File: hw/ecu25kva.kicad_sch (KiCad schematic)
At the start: 0 parts

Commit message: Wire the root sheet: the project has a netlist for the first time
Ten sheets each passed their own netlist and the project had none. The
root sheet's ten sheet symbols carried NO hierarchical pins, so a net
name appearing on two sheets was two nets and nothing compared them --
the cross-sheet audit in the last commit was a name comparison, not a
connectivity check.

Each symbol now carries one pin per net its child exports, read OUT of
the child rather than declared in a second list that could drift: 162
pins across the ten, each with a stub and a label. Two labels with the
same name are one net, which is how 162 pins connect without routing
162 wires across a page nobody could read.

Exporting it found the other half of the same problem immediately.
kicad-cli reported annotation errors: every sheet generator allocated
R1, C1, U1 from its own counter, so ten sheets had ten parts called R1.
schlib.REF_BASE gives each sheet its own hundred -- KiCad's own
sheet-number x 100 convention, applied at generation time instead of by
a hand pass in Eeschema. 196 components, no duplicate reference.

hw/check_netlist.py is the gate, and the counterpart to sim/run_sim.py:
that one guards the component values, this one guards the connectivity.
Same rule -- an exemption is not a pass. Every single-pin net is listed
with its reason, and a net that STOPS being single-pin fails the check
until it is removed from the list. An open item that quietly closes is
as much a drift as one that quietly opens.

  196 components, every reference unique
  113 named nets carrying two or more pins
   18 named nets reaching one pin, each a recorded open item
      GND 134 pins, 3V3_MCU 27, VBAT_PROT 12 -- all spanning the project

The root sheet carries those eighteen on the page itself, grouped by
what they wait on, so a reader does not have to run a script to find
which ends are loose.

Full set plots to docs/pdf/ECU-Schematics.pdf, 11 pages.

Two rendering bugs fixed: sheet pin names and their stu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
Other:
- sheet can ports: added CAN1_H, CAN1_L, CAN1_RX, CAN1_TX, CAN2_H, CAN2_L, CAN2_RX, CAN2_TX; removed none
- sheet connector ports: added BOOST_P_IN, BOOST_T_IN, CAM_FREQ_46, CAM_GND_44, CAN1_H, CAN1_L, CAN2_H, CAN2_L, COOLANT_T_IN, CRANK_HI_52, CRANK_LO_74, EGR_HIGH_59, EGR_LOW_81, EGR_POS_IN, EXC_BOOST_11, EXC_CAM_45, EXC_EGR_15, EXC_OIL_39, EXC_RAIL_32, INJ_A_03, INJ_B_05, INJ_LS1_73, INJ_LS2_29, INJ_LS3_07, IN_AUDIO_ABORT_H, IN_IGNITION_H, IN_OVERRIDE_SS_H, MU_RETURN, OIL_P_IN, RAIL_P_IN, RLY_BUZZER_OUT, RLY_MAIN_OUT, SGND_34, SGND_36, SHIELD_30, SW_COOLANT_C, SW_DROOP_C, VBAT_IN, V_BAT_1R, V_BAT_2R; removed none
- sheet discrete_io ports: added IN_AUDIO_ABORT, IN_AUDIO_ABORT_H, IN_IGNITION, IN_IGNITION_H, IN_OVERRIDE_SS, IN_OVERRIDE_SS_H, RLY_BUZZER, RLY_BUZZER_OUT, RLY_MAIN, RLY_MAIN_OUT, SW_COOLANT, SW_COOLANT_C, SW_DROOP, SW_DROOP_C, TRIP_LOOP, TRIP_SENSE, VBAT_PROT; removed none
- sheet injector ports: added GATE_KILL, INJ_A_03, INJ_B_05, INJ_HS_A, INJ_HS_B, INJ_LS1_73, INJ_LS2_29, INJ_LS3_07, INJ_LS_1, INJ_LS_2, INJ_LS_3, VBAT_PROT; removed none
- sheet mcu ports: added 3V3_MCU, BARO, BOOST_P, BOOST_T, CAM_EDGE, CAN1_RX, CAN1_TX, CAN2_RX, CAN2_TX, COOLANT_T, CRANK_EDGE, EGR_IN1, EGR_IN2, EGR_POS, GATE_KILL, INJ_HS_A, INJ_HS_B, INJ_LS_1, INJ_LS_2, INJ_LS_3, IN_AUDIO_ABORT, IN_IGNITION, IN_OVERRIDE_SS, ISNS_EGR, ISNS_INJ_A, ISNS_INJ_B, ISNS_MU, MU_PWM, OIL_P, RAIL_P, RLY_BUZZER, RLY_MAIN, SENSOR_5V_MON, SW_COOLANT, SW_DROOP, TRIP_SENSE, VBAT_PROT, V_BAT_1R_SNS, V_BAT_2R_SNS; removed none
- sheet metering_egr ports: added GATE_KILL, MU_PWM, MU_RETURN, VBAT_PROT; removed none
- sheet power_input ports: added VBAT_IN, VBAT_PROT; removed none
- sheet rails ports: added 3V3_MCU, 5V_SENSOR_A, 5V_SENSOR_B, 5V_SENSOR_C, SENSOR_5V_MON, VBAT_PROT; removed none
- sheet sensors_analog ports: added 5V_SENSOR_A, 5V_SENSOR_B, 5V_SENSOR_C, BOOST_P, BOOST_P_IN, BOOST_T, BOOST_T_IN, COOLANT_T, COOLANT_T_IN, EGR_POS, EGR_POS_IN, EXC_BOOST_11, EXC_CAM_45, EXC_EGR_15, EXC_OIL_39, EXC_RAIL_32, OIL_P, OIL_P_IN, RAIL_P, RAIL_P_IN, SGND_34, SGND_36, V_BAT_1R, V_BAT_1R_SNS, V_BAT_2R, V_BAT_2R_SNS; removed none
- sheet speed_inputs ports: added CAM_EDGE, CAM_FREQ_46, CAM_GND_44, CRANK_EDGE, CRANK_HI_52, CRANK_LO_74, EXC_CAM_45, SHIELD_30; removed none
- note added: "WHAT THIS SHEET IS FOR, AND WHAT IT LEAVES OPEN This page is the only place the ten sheets are joined. Each sheet symbol carries one hierarchical pin per net its child exports, and each pin carries a stub with a label: two labels anywhere on this page with the same name are one net. Until 21 September 2026 the symbols carried no pins at all, which meant every sheet's own netlist was correct and t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"

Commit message: Check the project netlist, and fix the three things it caught
hw/check_netlist.py grew the two checks that found them, so neither can
come back quietly. It is the counterpart to sim/run_sim.py: that one
guards the component values, this one guards the connectivity.

5V_MAIN WAS FOUR NETS. The buck's 5 V output is a board rail -- both CAN
transceivers' VCC, the five difference amplifiers and the discrete
inputs' pull-ups run off it -- and it was a LOCAL label on every one of
those sheets. A local label stops at its sheet's edge, so three of the
four copies had no regulator on them. Each sheet's own netlist was
correct, which is exactly why ten clean per-sheet netlists never found
it. rails now exports it as a hierarchical label.

3V3_MCU WAS THREE. Same mechanism on can (both transceivers' VIO) and
speed_inputs, where the comparator's supply, both upper clamp diodes and
the bias divider sat on a five-pin net with no rail attached.

New check: any sheet-local net whose name shadows a project-wide net
name fails. That is the exact shape of both defects.

FIVE SUPPLY PINS HAD NO DECOUPLING CAPACITOR. The difference amplifiers
on sensors_analog were the only undecoupled supply pins on the board. No
simulation block was ever going to say so -- sensor_differential.cir
models an ideal amplifier with no supply pin at all. 100 nF each, at the
pin.

New check: walk every power_in pin in the project netlist and ask
whether a capacitor sits on the same net. 22 supply pins, all covered.
One documented exemption, the LM5164's BST pin, whose bootstrap
capacitor IS the net.

Gate now: 201 components with unique references, 108 named nets carrying
two or more pins, 18 reaching one and each a recorded open item, GND 139
pins, 3V3_MCU 36, 5V_MAIN 28, VBAT_PROT 12.

Schematic set re-plotted: docs/pdf/ECU-Schematics.pdf, 11 pages.
Suite still 24/24.

Co-Authored-By: Claude Opus 5 <noreply@anthropic.com>
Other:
- sheet can ports: added 3V3_MCU, 5V_MAIN; removed none
- sheet discrete_io ports: added 5V_MAIN; removed none
- sheet rails ports: added 5V_MAIN; removed none
- sheet sensors_analog ports: added 5V_MAIN; removed none
- sheet speed_inputs ports: added 3V3_MCU; removed none

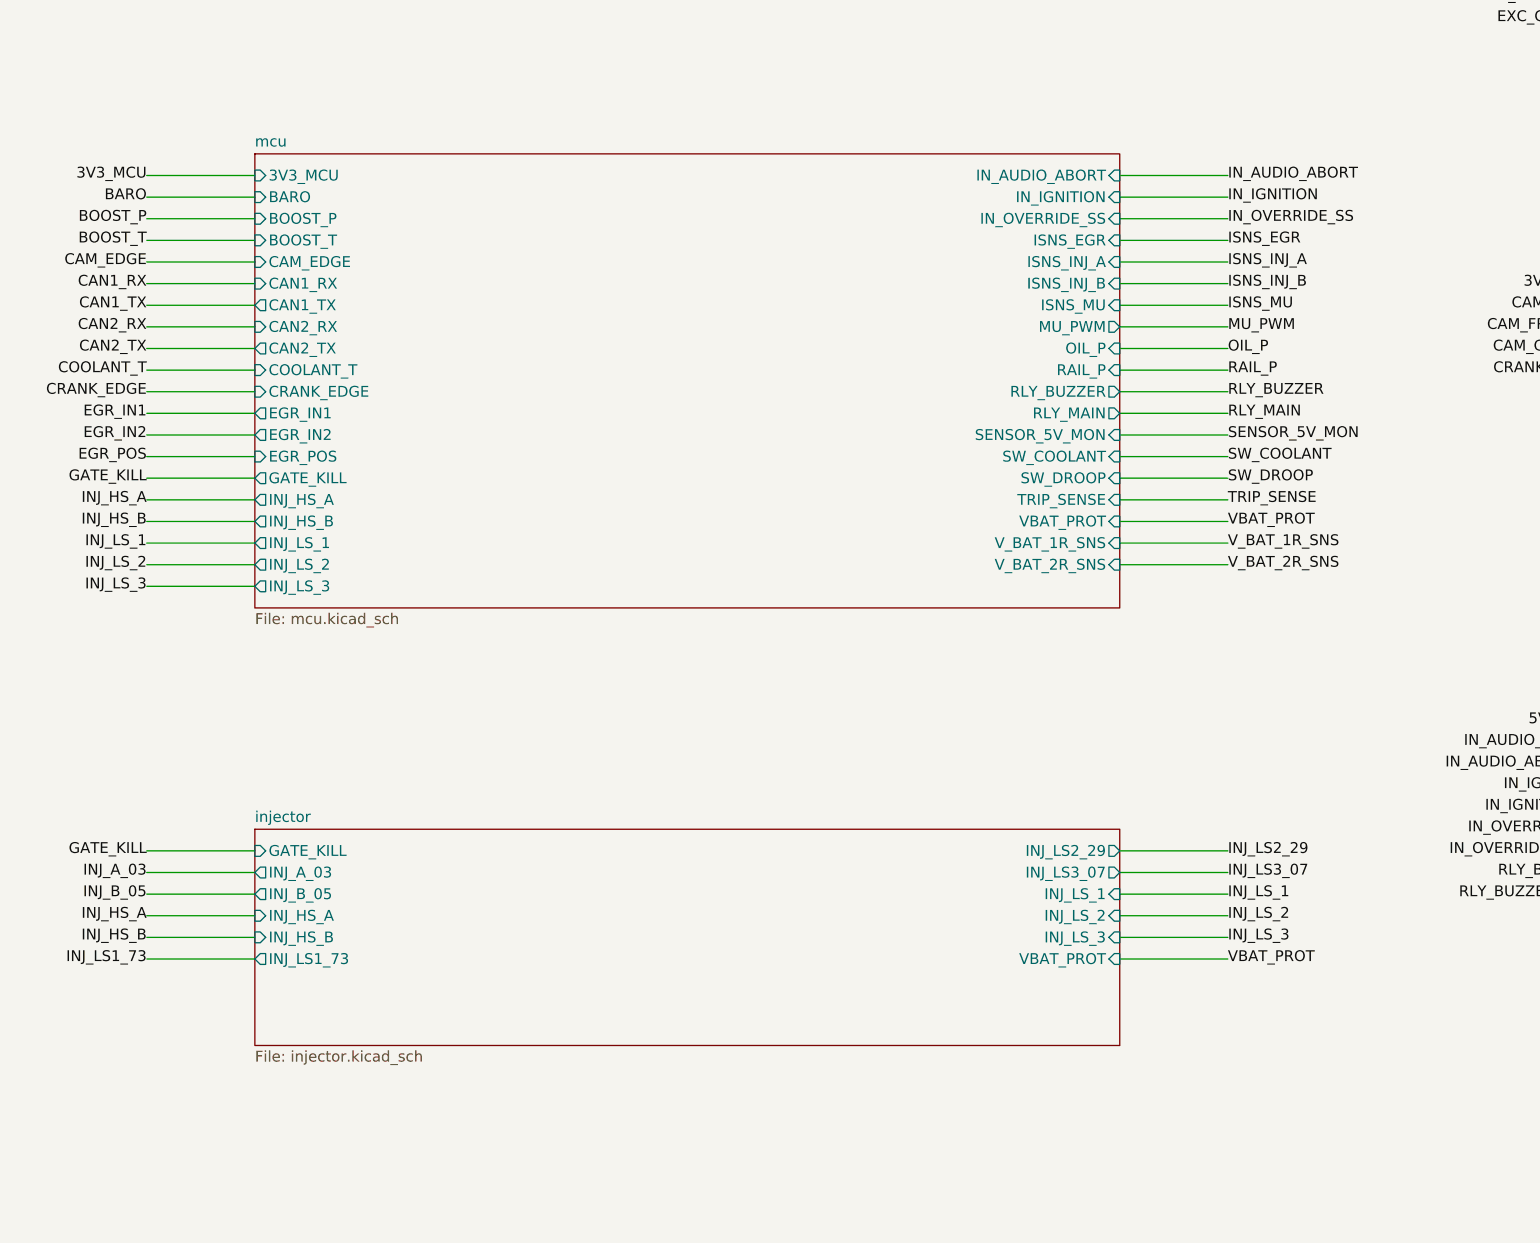
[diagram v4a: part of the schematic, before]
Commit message: Correct the injector high side: a diode-OR cannot be chopped or bootstrapped
Choosing a gate driver for the high side found an error in the sheet
drawn two commits ago. The bank node was fed from VBAT_PROT through a
plain diode-OR, with the LOW side chopping for hold, on the argument
that it needed no extra MCU pin. It is wrong three ways, and only the
third is visible from a datasheet -- which is why drawing it did not
catch it and choosing a part for it did.

1. IT CANNOT REGULATE HOLD. With the battery on a diode the only switch
   in the loop is the low side, and when the low side opens the coil's
   current has nowhere to go but the recirculation diode into the 100 V
   boost rail. That is a fast decay against -87 V -- turn-off, not
   chopping. Hold needs a slow freewheel around the coil.

2. IT LEAVES CONNECTOR PINS 03 AND 05 PERMANENTLY LIVE. A diode from
   the battery to a connector pin means a harness short to ground draws
   current whenever the battery is connected, with no switch anywhere
   to stop it.

3. THE GATE DRIVER CANNOT BE BOOTSTRAPPED. A bootstrap capacitor
   charges when the switch node goes LOW. A battery diode holds that
   node at 12.8 V, so it never does, and the high side's floating supply
   can never refresh.

What replaces it is what injector_turnoff.cir already models and spends
a paragraph of its header justifying: two high-side switches per bank
onto a common node -- boost rail for the peak phase, battery for hold --
plus D_fw from GROUND to that node. Hold chopping moves to the high
side, the node swings to -0.7 V on every off-time, and the bootstrap
charges. Both switches have their SOURCE on the bank node, so one
floating supply serves two gates.

The battery switch needs a series BLOCKING diode and would with either
polarity of FET: an N-channel's body diode points source to drain, so
with the bank at 100 V during the peak phase it would dump the boost
rail into the battery. It goes on the drain side, which leaves the FET's
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
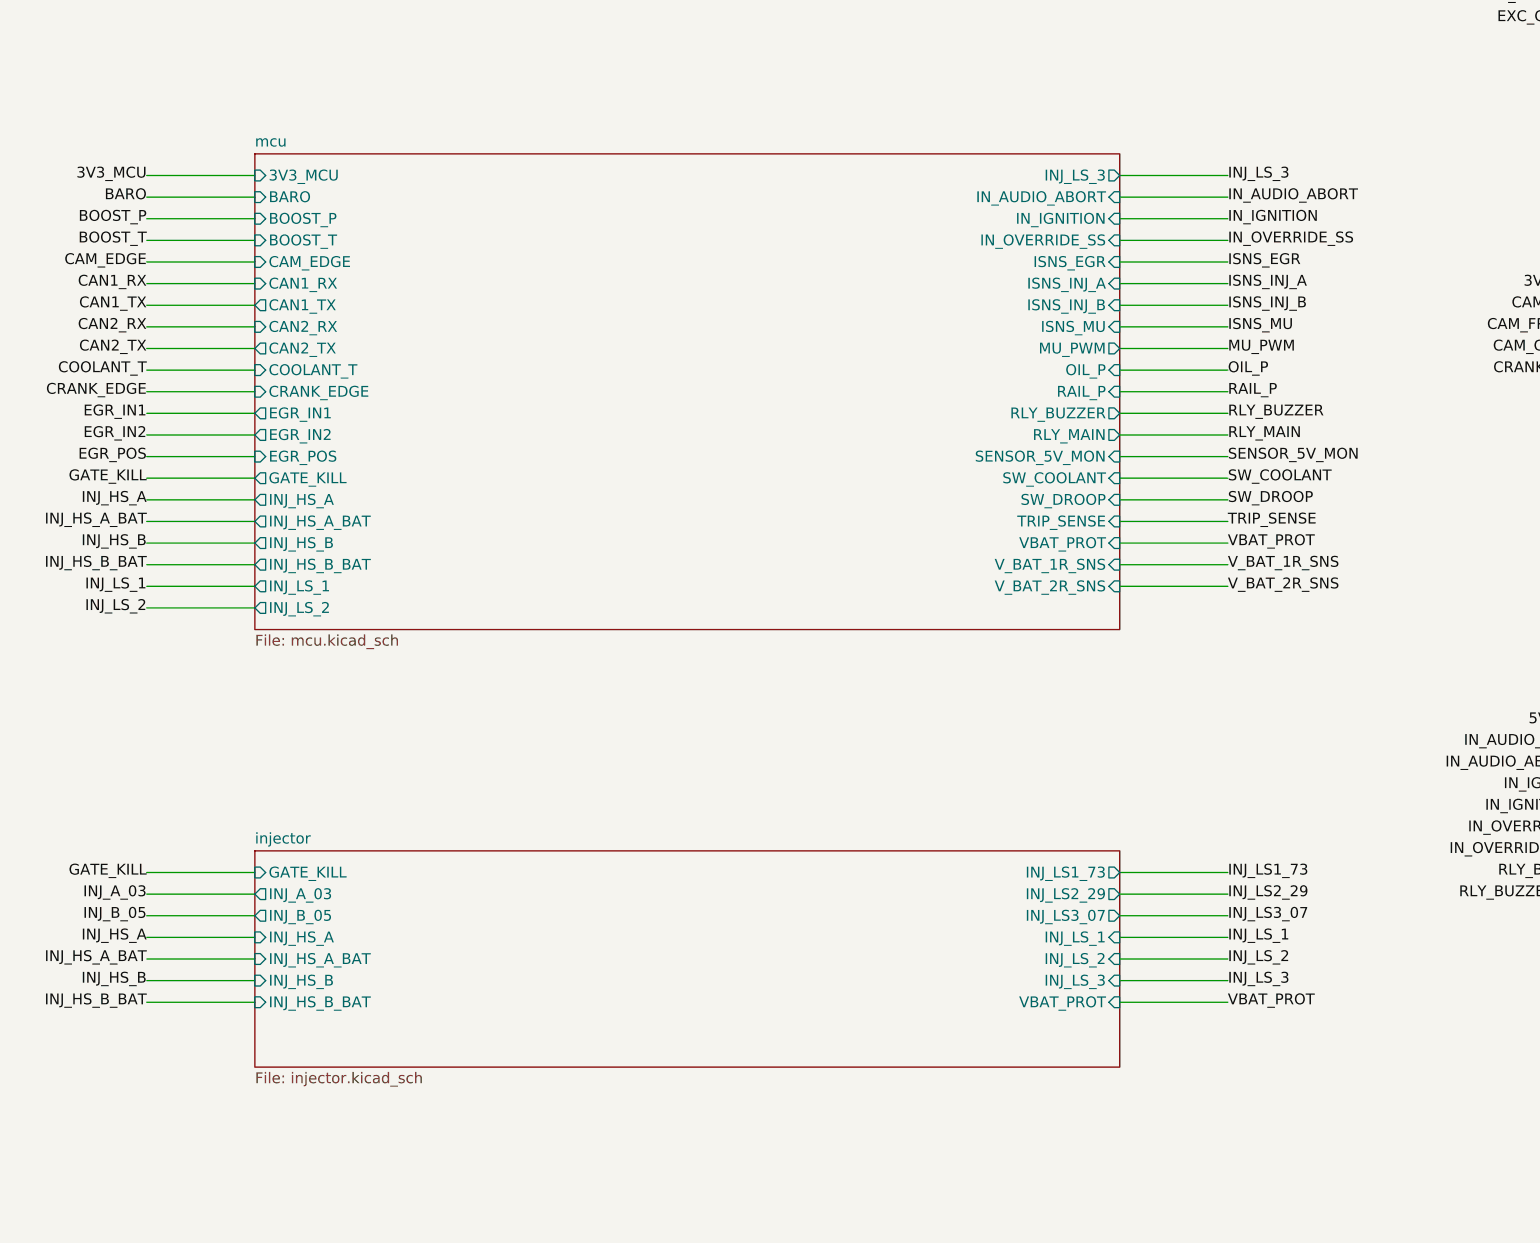
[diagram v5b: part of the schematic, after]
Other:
- sheet injector ports: added INJ_HS_A_BAT, INJ_HS_B_BAT; removed none
- sheet mcu ports: added INJ_HS_A_BAT, INJ_HS_B_BAT; removed none
